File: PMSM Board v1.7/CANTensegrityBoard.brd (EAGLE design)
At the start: 100.5 x 48 mm, 78 parts, among them IC1 DRV8303, U10 H1206T500R-10, U2 SN65HVD232_D_8, U3 SN65LVDT348_PW_1, U9 H1206T500R-10

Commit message: rerouting PMSM Board
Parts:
- added C14: 5600pF, SwitcherPowerStage:0805
- added C15: 270pF, SwitcherPowerStage:0805
- added C29: 47uF\, SwitcherPowerStage:C2220K
- added C30, C31, C32: 1uF, SwitcherPowerStage:0805
- added C5: 4.7uF, SwitcherPowerStage:1210
- added C6: .01uF, SwitcherPowerStage:0805
- added C8: .1uF, SwitcherPowerStage:0805
- added D1: DIODE-SCHOTTKY240A, SwitcherPowerStage:SMA-DIODE-B240A
- added R10: 59k, SwitcherPowerStage:0805
- added R11: 10k, SwitcherPowerStage:0805
- added R2: 348k, SwitcherPowerStage:0805
- added R3: 88.7k, SwitcherPowerStage:0805
- added R8: 237k, SwitcherPowerStage:0805
- added R9: 7.68k, SwitcherPowerStage:0805
- added U$13: SLF12555T, SwitcherPowerStage:SLF12555
- added U1: TPS73733-Q1_DRB_8, SwitcherPowerStage:DRB8_1P75X1P5
- added U4: TPS54240_DRC_10, SwitcherPowerStage:DRC10_2P4X1P65
- added U5: LP38692_NGG_6, SwitcherPowerStage:SDE06A
- C2, C4: device ASL:1206 -> ASL:0805
- moved C2 10.7 mm to (47.3, 18.2), turned to 0 degrees
- moved C1 10.1 mm to (47.3, 16.8), turned to 0 degrees
- moved C4 8.63 mm to (63.6, 18.0)
- moved C3 8.02 mm to (63.6, 16.6)
- moved IC1 8.00 mm to (55.2, 13.0)
- moved R1 8.00 mm to (46.2, 6.00)
- moved TP6 8.00 mm to (48.4, 8.18)
- moved TP7 8.00 mm to (48.5, 7.16)
- moved C19 8.00 mm to (63.0, 7.95)
- moved C11 7.89 mm to (59.2, 26.0)
- moved C10 7.82 mm to (55.3, 26.0)
- moved C9 7.80 mm to (51.5, 26.0)
- moved C16 7.00 mm to (52.8, 2.76)
- moved C17 7.00 mm to (54.6, 3.64)
- moved C18 7.00 mm to (60.1, 3.77)
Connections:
- new net N$10: C8.1, U4.1
- new net N$13: C8.2, D1.C, U$13.P$1, U4.10
- new net N$14: C15.1, R9.2, U4.8
- new net N$15: C14.1, R9.1
- new net N$16: R10.1, R11.2, U4.7
- new net N$7: R2.1, R3.2, U4.3
- new net N$8: C6.1, U4.4
- new net N$9: R8.2, U4.5
- new net VCC5V0: C31.1, U1.5, U1.8, U5.4, U5.5
- new net VCC5V5: C29.1, C30.1, R10.2, U$13.P$2, U5.1, U5.3, U5.6
- net GND: now also C14.2, C15.2, C29.2, C30.2, C31.2, C32.2, C5.2, C6.2, D1.A, R11.1, R3.1, R8.1, U1.4, U1.9, U4.9, U4.P$1, U4.P$2, U4.P$3, U4.P$4, U4.P$5, U5.2, U5.7
- net PVDD: now also C5.1, R2.2, U4.2
- net VCC3V3: now also C32.1, U1.1
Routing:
- net PWM2L: track 78.6 -> 0.00 mm, vias 3 -> 0
- net PVDD: track 87.4 -> 12.0 mm, vias 3 -> 0
- net CRNT2: track 73.5 -> 0.00 mm, vias 2 -> 0
- net GH_A: track 73.0 -> 0.00 mm, vias 2 -> 0
- net SL_A: track 72.2 -> 0.00 mm, vias 3 -> 0
- net CRNT1: track 68.6 -> 0.00 mm, vias 2 -> 0
- net GL_A: track 67.4 -> 0.00 mm, vias 3 -> 0
- net GH_C: track 66.0 -> 0.00 mm, vias 4 -> 0
- net PWM3H: track 62.8 -> 0.00 mm, vias 2 -> 0
- net GH_B: track 60.4 -> 0.06 mm, vias 3 -> 0
- net SN1: track 66.5 -> 6.62 mm, vias 3 -> 0
- net PWM3L: track 58.6 -> 0.00 mm, vias 2 -> 0
- net EN_GATE: track 57.5 -> 0.00 mm, vias 2 -> 0
- net GL_C: track 55.9 -> 0.00 mm, vias 2 -> 0
- net PWM1L: track 55.3 -> 0.00 mm, vias 3 -> 0
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- removed copper zone on layer 1, net VCC3V3
- removed copper zone on layer 16, net VCC3V3

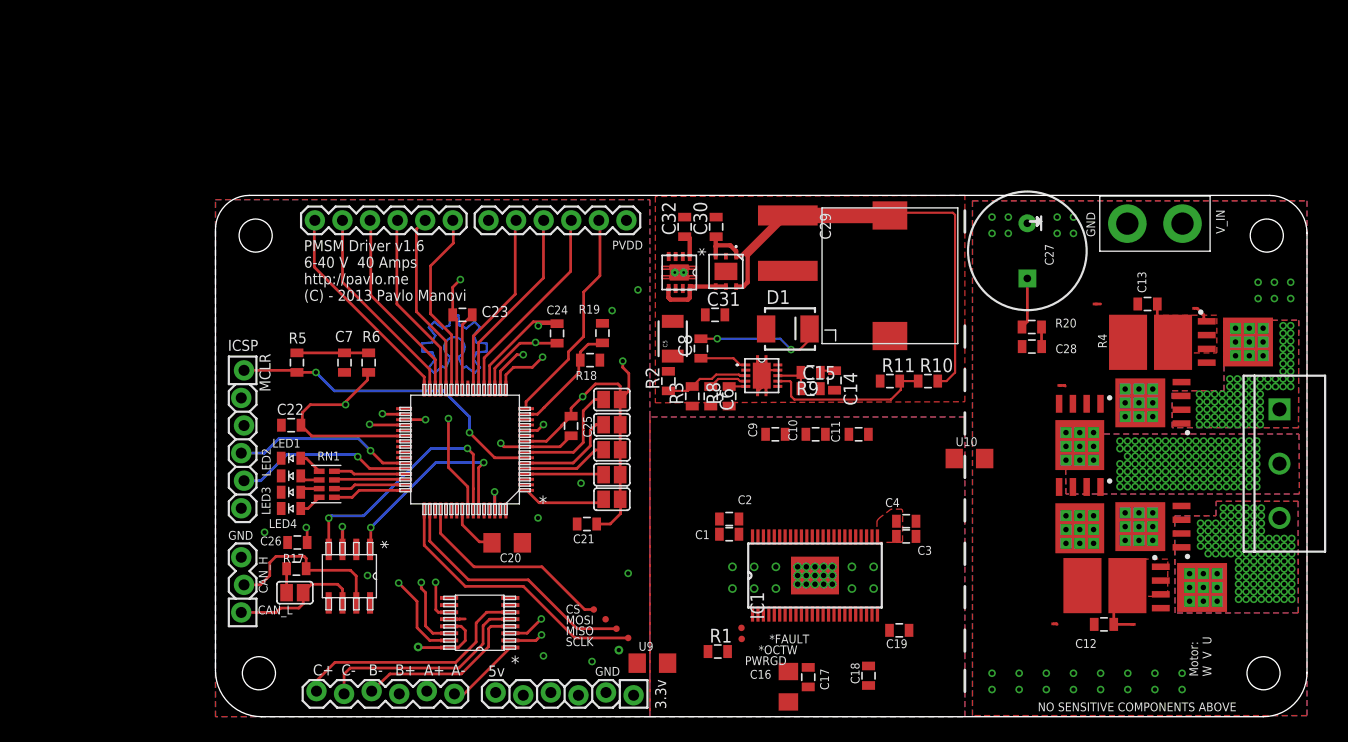
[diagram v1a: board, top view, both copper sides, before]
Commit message: Started making room for connectors
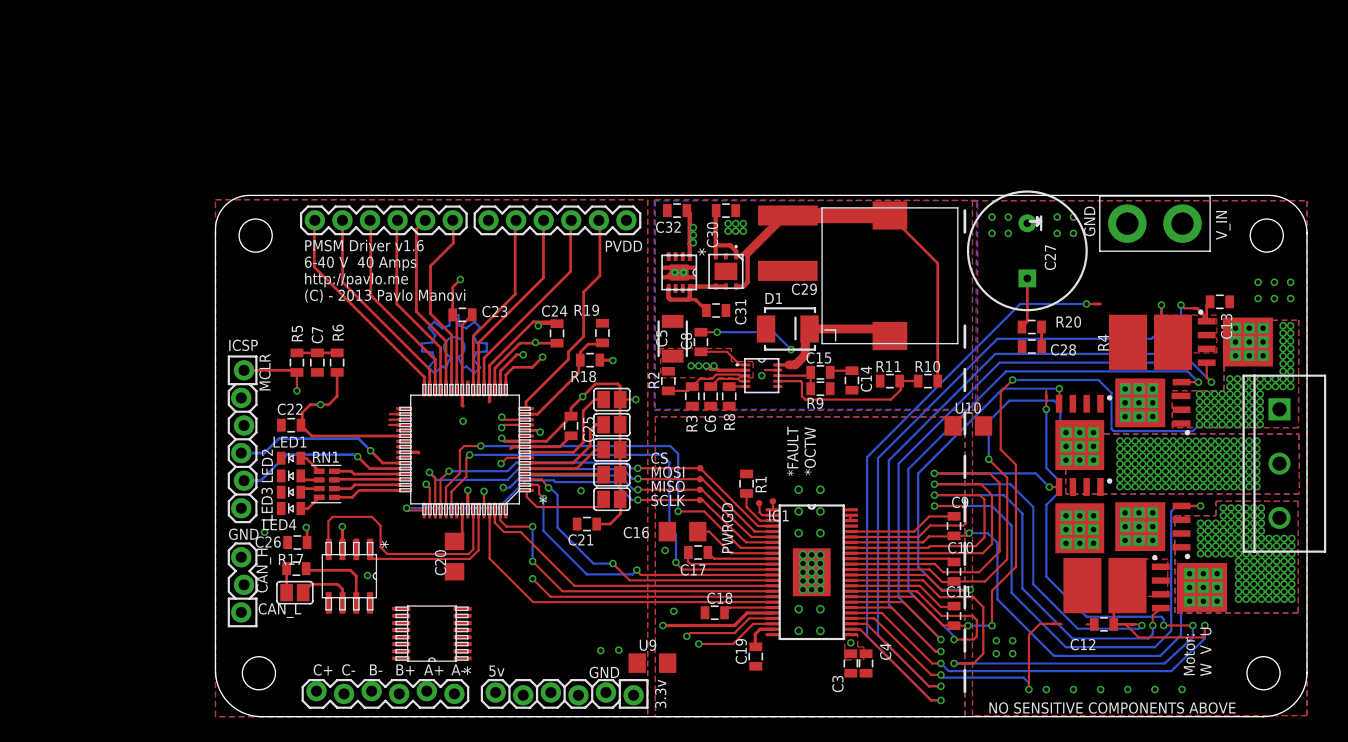
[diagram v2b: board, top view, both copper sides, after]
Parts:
- removed C1: .1 uF 100V, ASL:0805
- removed C2: 2.2uF 100V, ASL:0805
- moved C11 18.9 mm to (68.0, 9.28), turned to 270 degrees
- moved C9 18.5 mm to (68.0, 17.6), turned to 270 degrees
- moved C10 18.0 mm to (68.0, 13.3), turned to 270 degrees
- moved C16 17.3 mm to (43.0, 17.0), turned to 180 degrees
- moved TP1 16.3 mm to (44.6, 22.9)
- moved R1 15.7 mm to (48.9, 21.4), turned to 270 degrees
- moved TP2 15.6 mm to (44.6, 21.9)
- moved C17 15.3 mm to (44.4, 15.1), turned to 180 degrees
- moved C18 15.3 mm to (46.0, 9.57), turned to 0 degrees
- moved TP3 14.9 mm to (44.6, 20.9)
- moved TP4 14.3 mm to (44.6, 19.9)
- moved C4 13.6 mm to (59.9, 4.90), turned to 270 degrees
- moved C19 13.4 mm to (49.8, 5.54), turned to 90 degrees
- moved C3 12.8 mm to (58.5, 4.90), turned to 270 degrees
- moved TP7 12.6 mm to (50.1, 19.6), turned to 270 degrees
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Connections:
- removed net N$11: C9.2, IC1.42
- removed net VCC5V: JP5.6
- net DRV_GND: no longer C1.2, C2.2
- net GND: no longer C14.2, C15.2, C29.2, C30.2, C31.2, C32.2, C5.2, C6.2, D1.A, R11.1, R3.1, R8.1, U1.4, U1.9, U4.9, U4.P$1, U4.P$2, U4.P$3, U4.P$4, U4.P$5, U5.2, U5.7
- net PGND: now also C14.2, C15.2, C29.2, C30.2, C31.2, C32.2, C5.2, C6.2, D1.A, R11.1, R3.1, R8.1, U1.4, U1.9, U1.P$1, U1.P$2, U1.P$3, U1.P$4, U4.9, U5.2, U5.7
- net PVDD: no longer C1.1, C2.1
- net SH_A: now also C9.2, IC1.42
- net VCC5V0: now also JP5.6
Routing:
- net SL_B: track 0.00 -> 77.8 mm, vias 0 -> 4
- net SN2: track 5.99 -> 75.7 mm, vias 0 -> 2
- net GH_C: track 0.00 -> 66.3 mm, vias 0 -> 2
- net SL_C: track 0.00 -> 66.1 mm, vias 0 -> 2
- net SP2: track 0.00 -> 63.5 mm, vias 0 -> 2
- net GL_C: track 0.00 -> 63.0 mm, vias 0 -> 2
- net GH_A: track 0.00 -> 62.6 mm, vias 0 -> 2
- net SH_C: track 0.00 -> 60.1 mm, vias 77 -> 80
- net GL_A: track 0.00 -> 54.1 mm, vias 0 -> 2
- net SL_A: track 0.00 -> 53.3 mm, vias 0 -> 2
- net CRNT2: track 0.00 -> 47.1 mm, vias 0 -> 2
- net CRNT1: track 0.00 -> 46.2 mm, vias 0 -> 2
- net SN1: track 6.62 -> 52.6 mm, vias 0 -> 2
- net SH_A: track 0.00 -> 44.0 mm, vias 116 -> 118
- net GL_B: track 0.00 -> 43.6 mm, vias 0 -> 2
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
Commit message: More redesign work for v1.7
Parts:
- removed J2: (no value), ASL:1X02_XTRA_BIG
- removed JP1, JP2: (no value), ASL:1X06
- removed JP5: (no value), CMPE118lib:1X06_LOCK
- removed JP6: M03LOCK, ASL:1X03_LOCK
- removed JP7: M03-SCREW-5MM, pavlo:SCREWTERMINAL-5MM-3
- removed JP8: (no value), ASL:1X06-SIP_LOCK
- added U$14, U$19: MICROCLASP3, OpenPMSM:55932-0310
- added U$15: 3M10PIN2500, OpenPMSM:FOUR-WALL-2500-LP-STH
- added U$16: MINIFITJR4PIN, OpenPMSM:0039288040
- added U$17: MINIFITJR6PIN, OpenPMSM:0039288060
- added U$18: MICROCLASP2, OpenPMSM:55932-0210
- added U$20: MICROCLASP5, OpenPMSM:55932-0510
- moved SJ8 61.2 mm to (43.5, 60.8)
- moved R17 56.0 mm to (39.1, 59.9), turned to 270 degrees
- moved U3 55.1 mm to (31.8, 61.5)
- moved C22 26.6 mm to (7.87, 53.4)
- moved SJ7 22.8 mm to (16.5, 40.1), turned to 270 degrees
- moved SJ1 22.7 mm to (25.9, 40.1), turned to 270 degrees
- moved SJ6 22.0 mm to (18.9, 40.1), turned to 270 degrees
- moved SJ4 22.0 mm to (23.6, 40.1), turned to 270 degrees
- moved SJ5 21.7 mm to (21.3, 40.1), turned to 270 degrees
- moved U9 20.8 mm to (40.6, 25.7)
- moved LED4 20.4 mm to (26.7, 14.3), turned to 270 degrees
- moved LED3 19.3 mm to (25.2, 14.3), turned to 270 degrees
- moved LED2 18.5 mm to (23.7, 14.3), turned to 270 degrees
- moved C7 18.4 mm to (2.98, 49.9)
- moved R5 18.4 mm to (1.10, 49.9)
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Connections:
- net AN4: no longer JP5.4
- net AN5: no longer JP5.5
- net CAN_H: no longer JP6.2
- net CAN_L: no longer JP6.1
- net EN_A+: no longer JP8.2
- net EN_A-: no longer JP8.1
- net EN_B+: no longer JP8.3
- net EN_B-: no longer JP8.4
- net EN_C+: no longer JP8.6
- net EN_C-: no longer JP8.5
- net GND: no longer JP2.6, JP5.2, JP6.3
- net N$48: no longer JP1.6
- net N$49: no longer JP1.5
- net N$50: no longer JP1.4
- net N$51: no longer JP1.3
- net N$52: no longer JP1.2
- net N$53: no longer JP1.1
- net N$55: no longer JP2.2
- net N$56: no longer JP2.3
- net N$57: no longer JP2.4
- net N$58: no longer JP2.5
- net PGND: no longer J2.1
- net PVDD: no longer J2.2, JP2.1
- net RA11: no longer JP5.3
- net SH_A: no longer JP7.3
- net SH_B: no longer JP7.2
- net SH_C: no longer JP7.1
- net VCC3V3: no longer JP5.1
- net VCC5V0: no longer JP5.6
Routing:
- net VCC3V3: track 89.3 -> 17.3 mm, vias 13 -> 4
- net AN5: track 38.3 -> 0.00 mm, vias 1 -> 0
- net AN4: track 37.9 -> 0.00 mm, vias 1 -> 0
- net PWM3H: track 34.5 -> 0.00 mm, vias 2 -> 0
- net PWM3L: track 32.2 -> 0.00 mm
- net MCLR: track 31.7 -> 0.00 mm, vias 2 -> 0
- net PWM2L: track 30.6 -> 0.00 mm, vias 2 -> 0
- net GND: track 29.2 -> 0.00 mm, vias 6 -> 0
- net PWM2H: track 29.2 -> 0.00 mm
- net RA11: track 28.8 -> 0.00 mm, vias 2 -> 0
- net DC_CAL: track 42.1 -> 16.5 mm, vias 2 -> 1
- net EN_GATE: track 43.2 -> 19.7 mm, vias 2 -> 1
- net CANRX: track 22.5 -> 0.00 mm
- net MOSI: track 38.5 -> 16.2 mm, vias 2 -> 1
- net SCLK: track 38.9 -> 16.9 mm, vias 2 -> 1
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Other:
- board text removed: "5v"
- board text removed: "A+"
- board text removed: "A-"
- board text removed: "B+"
- board text removed: "B-"
- board text removed: "C+"
- board text removed: "C-"

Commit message: Almost done with v1.7~
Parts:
- removed SJ4, SJ5, SJ6, SJ7: (no value), jumper:SJ
- removed U$1: DSPIC33EP128MC502-I/SS, pavlo:QFP64-10X10MC
- added U6: DSPIC33EP256MU80, OpenPMSM:QFP64-10X10MC
- moved U3 50.5 mm to (14.3, 14.1), turned to 90 degrees
- moved SJ8 41.7 mm to (15.1, 30.3), turned to 90 degrees
- moved R17 39.5 mm to (12.9, 30.4), turned to 90 degrees
- moved SJ1 28.7 mm to (-2.62, 36.5)
- moved LED1 26.5 mm to (27.6, 40.3), turned to 90 degrees
- moved LED4 26.2 mm to (23.1, 40.3), turned to 90 degrees
- moved LED2 26.1 mm to (26.1, 40.3), turned to 90 degrees
- moved LED3 26.0 mm to (24.6, 40.3), turned to 90 degrees
- moved C24 22.2 mm to (24.8, 14.1), turned to 270 degrees
- moved U2 20.2 mm to (15.7, 35.3), turned to 180 degrees
- moved C20 19.4 mm to (22.6, 11.9), turned to 270 degrees
- moved C26 19.0 mm to (27.6, 32.7), turned to 90 degrees
- moved U$20 18.5 mm to (3.70, 18.1), turned to 90 degrees
- moved C21 18.5 mm to (23.3, 32.7), turned to 90 degrees
- moved RN1 17.7 mm to (24.2, 36.0), turned to 0 degrees
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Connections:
- removed net AN4: U$1.17
- removed net AN5: U$1.18
- removed net EN_A: U$1.36, U3.15
- removed net EN_A+: U3.2
- removed net EN_A-: U3.1
- removed net EN_B: U$1.35, U3.14
- removed net EN_B+: U3.3
- removed net EN_B-: U3.4
- removed net EN_C: U$1.34, U3.11
- removed net EN_C+: U3.6
- removed net EN_C-: U3.5
- removed net N$26: U$1.37
- removed net N$27: SJ4.2, U$1.4
- removed net N$28: SJ5.2, U$1.5
- removed net N$29: SJ6.2, U$1.6
- removed net N$30: SJ7.2, U$1.8
- removed net N$33: RN1.P$1, U$1.48
- removed net N$41: RN1.P$2, U$1.47
- removed net N$42: RN1.P$3, U$1.46
- removed net N$43: RN1.P$4, U$1.45
- removed net N$48: U$1.32
- removed net N$49: U$1.31
- removed net N$50: U$1.30
- removed net N$51: U$1.29
- removed net N$52: U$1.28
- removed net N$53: U$1.27
- removed net N$55: U$1.16
- removed net N$56: U$1.21
- removed net N$57: U$1.22
- removed net N$58: U$1.23
- removed net RA11: U$1.12
- removed net RA12: U$1.11
- removed net RC9: U$1.55
- new net CH_A+: U$15.6, U3.6
- new net CH_A-: U$15.5, U3.5
- new net CH_B+: U$15.4, U3.3
- new net CH_B-: U$15.3, U3.4
- new net CH_I+: U$15.2, U3.2
- new net CH_I-: U$15.1, U3.1
- new net HALL1: U$20.3, U6.44
- new net HALL2: U$20.4, U6.43
- new net HALL3: U$20.5, U6.42
- new net LED1: RN1.P$4, U6.21
- new net LED2: RN1.P$3, U6.22
- new net LED3: RN1.P$2, U6.23
- new net LED4: RN1.P$1, U6.24
- new net QEI_A: U3.15, U6.55
- new net QEI_B: U3.14, U6.54
- new net QEI_I: U3.11, U6.53
- net *SCS: now also U6.8; no longer U$1.52
- net CANRX: now also U6.31; no longer U$1.58
- net CANTX: now also U6.32; no longer U$1.59
- net CRNT1: now also U6.27; no longer U$1.13
- net CRNT2: now also U6.28; no longer U$1.14
- net DC_CAL: now also U6.6; no longer U$1.53
- net EN_GATE: now also U6.5; no longer U$1.54
- net GND: now also U$15.7, U$20.2, U6.20, U6.25, U6.41, U6.9; no longer U$1.20, U$1.25, U$1.41, U$1.9
- net MCLR: now also U6.7; no longer U$1.7
- net MISO: now also U6.3; no longer U$1.50
- net MOSI: now also U6.4; no longer U$1.51
- net N$25: now also U6.15; no longer U$1.15
- net N$31: now also U6.56; no longer U$1.56
- net N$5: now also U6.38; no longer SJ1.2, U$1.1
- net PGC: now also U6.18; no longer U$1.44
- net PGD: now also U6.17; no longer U$1.43
- net PWM1H: now also U6.1; no longer U$1.2
- net PWM1L: now also U6.64; no longer U$1.3
- net PWM2H: now also U6.63; no longer U$1.62
- net PWM2L: now also U6.62; no longer U$1.63
- net PWM3H: now also U6.61; no longer U$1.60
- net PWM3L: now also U6.60; no longer U$1.61
- net SCLK: now also U6.2; no longer U$1.49
- net VCC3V3: now also U$20.1, U6.10, U6.19, U6.26, U6.57; no longer SJ1.1, SJ4.1, SJ5.1, SJ6.1, SJ7.1, U$1.10, U$1.19, U$1.26, U$1.38, U$1.57
- net VCC5V0: now also U$15.10
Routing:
- net MCLR: track 0.00 -> 43.3 mm, vias 0 -> 1
- net VCC3V3: track 17.3 -> 55.1 mm, vias 4 -> 10
- net PWM3L: track 0.00 -> 29.9 mm
- net PWM3H: track 0.00 -> 29.1 mm
- net PGD: track 0.00 -> 28.9 mm, vias 0 -> 1
- net PWM2L: track 0.00 -> 28.2 mm
- net PWM2H: track 0.00 -> 27.4 mm
- net PGC: track 0.00 -> 25.4 mm, vias 0 -> 1
- net CRNT2: track 29.5 -> 53.0 mm, vias 1 -> 2
- net CRNT1: track 29.1 -> 49.5 mm, vias 1 -> 2
- net HALL1: track 0.00 -> 16.9 mm
- net HALL2: track 0.00 -> 16.2 mm
- net DC_CAL: track 16.5 -> 32.7 mm, vias 1 -> 2
- net QEI_A: track 0.00 -> 16.2 mm
- net HALL3: track 0.00 -> 15.6 mm
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- added copper zone on layer 15, net GND
- added copper zone on layer 2, net GND
- added copper zone on layer 15, net VCC5V0
- added copper zone on layer 15, net VCC5V5
- removed copper zone on layer 15, net VCC3V3
